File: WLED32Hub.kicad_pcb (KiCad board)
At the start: 2 copper layers, 112.4 x 137.2 mm, 60 parts, among them J1 USB_C_Receptacle_PowerOnly_6P, J10 WAGO, J11 WAGO, J12 WAGO, J13 WAGO, J14 WAGO, J15 WAGO, J16 WAGO, J17 WAGO, J18 WAGO, J19 Conn_01x05, J2 Power WAGO, J3 WAGO, J4 WAGO, J5 WAGO, J6 WAGO, J7 WAGO, J8 WAGO, J9 WAGO, Q1 IRLB8721PBF, Q10 IRLB8721PBF, Q11 IRLB8721PBF, Q12 IRLB8721PBF, Q13 IRLB8721PBF, Q14 IRLB8721PBF, Q15 IRLB8721PBF, Q16 IRLB8721PBF, Q2 IRLB8721PBF, Q3 IRLB8721PBF, Q4 IRLB8721PBF, Q5 IRLB8721PBF, Q6 IRLB8721PBF, Q7 IRLB8721PBF, Q8 IRLB8721PBF, Q9 IRLB8721PBF, U1 ESP32-DevKit-V3.0, U2 Arduino-Pro-Micro

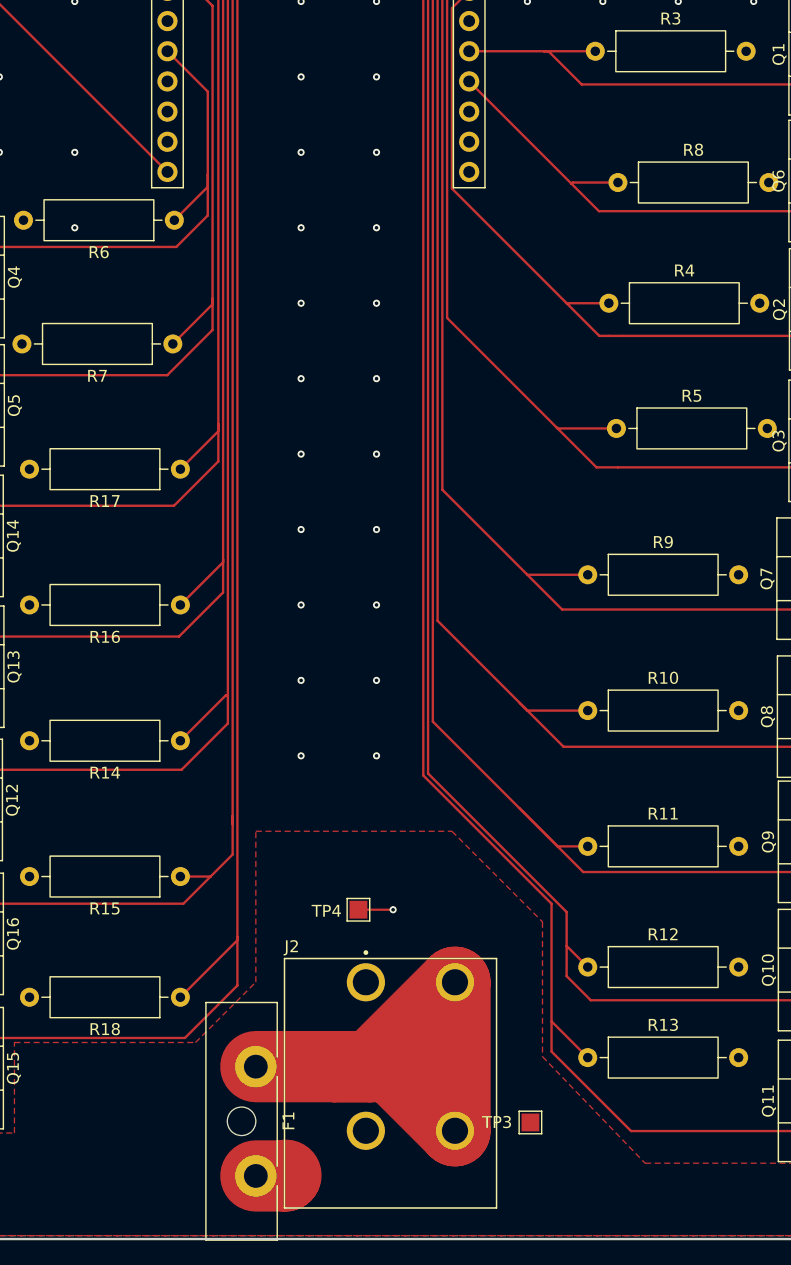
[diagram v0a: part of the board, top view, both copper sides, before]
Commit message: Adding Test Points to LED Switching Signals
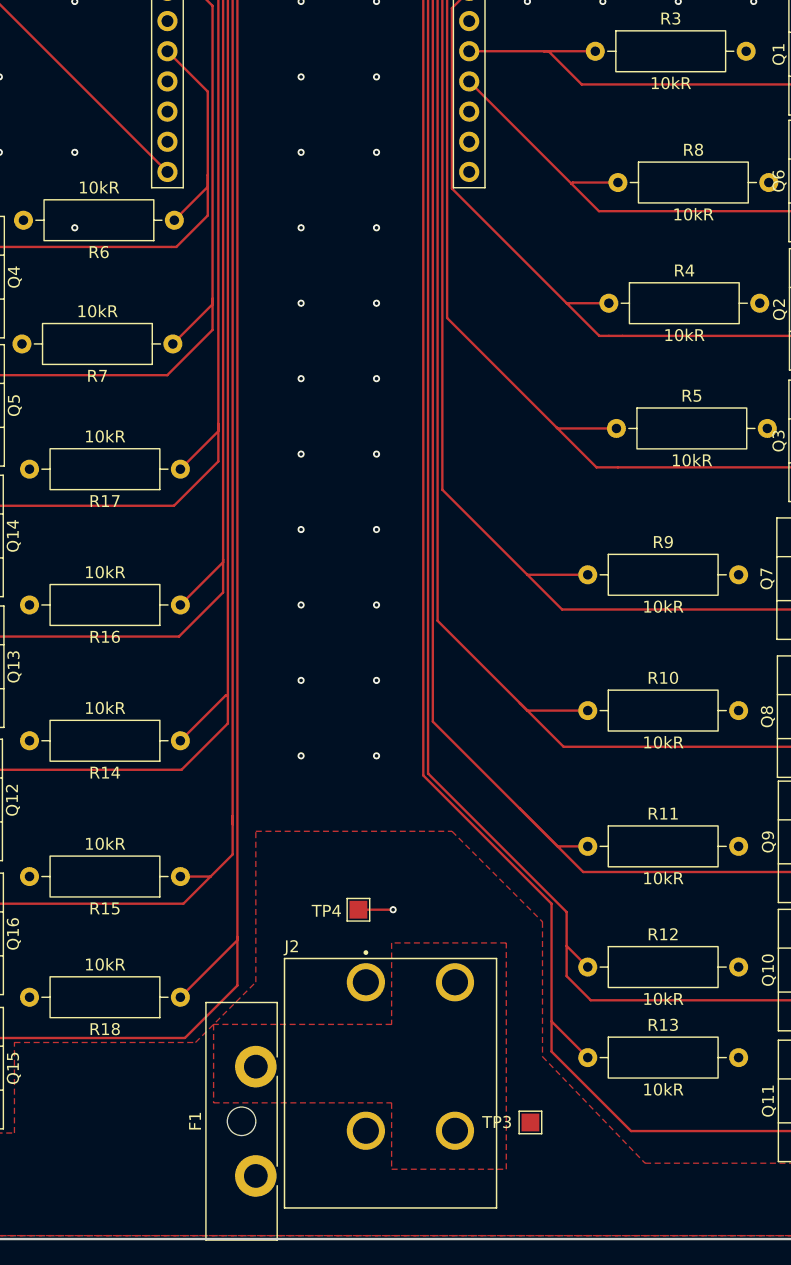
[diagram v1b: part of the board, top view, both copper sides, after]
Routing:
- net Net-(J2-Pin_1): track 44.6 -> 0.00 mm
- net VLED: track 2.56 -> 0.00 mm
- added copper zone on F.Cu, net Net-(J2-Pin_1)
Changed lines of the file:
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@@
 		(property "Value" "10kR"
 			(at 6.35 2.72 0)
-			(layer "F.Fab")
+			(layer "F.SilkS")
 			(effects
 				(font
@@
 		(property "Value" "10kR"
 			(at 6.35 2.72 0)
-			(layer "F.Fab")
+			(layer "F.SilkS")
 			(effects
 				(font
@@
 		(property "Value" "10kR"
 			(at 6.35 2.72 0)
-			(layer "F.Fab")
+			(layer "F.SilkS")
 			(effects
 				(font
@@
 		(property "Value" "10kR"
 			(at 6.35 2.72 0)
-			(layer "F.Fab")
+			(layer "F.SilkS")
 			(effects
 				(font
@@
 		(property "Value" "10kR"
 			(at 6.35 2.72 0)
-			(layer "F.Fab")
+			(layer "F.SilkS")
 			(effects
 				(font
@@
 		(property "Value" "10kR"
 			(at 6.35 2.72 0)
-			(layer "F.Fab")
+			(layer "F.SilkS")
 			(effects
 				(font
@@
 		(tags "Fuseholder ATO Blade littelfuse Pudenz 2 Pin")
 		(property "Reference" "F1"
-			(at 4.57 -2.78 90)
+			(at 4.595 5.08 90)
 			(layer "F.SilkS")
 			(effects
@@
 		(property "Value" "10kR"
 			(at 6.35 2.72 0)
-			(layer "F.Fab")
+			(layer "F.SilkS")
 			(effects
 				(font
@@
 		(property "Value" "10kR"
 			(at 6.35 2.72 0)
-			(layer "F.Fab")
+			(layer "F.SilkS")
 			(effects
 				(font
@@
 		(property "Value" "10kR"
 			(at 6.35 2.72 0)
-			(layer "F.Fab")
+			(layer "F.SilkS")
 			(effects
 				(font
@@
 		(property "Value" "10kR"
 			(at 6.35 2.72 0)
-			(layer "F.Fab")
+			(layer "F.SilkS")
 			(effects
 				(font
@@
 		(property "Value" "10kR"
 			(at 6.35 2.72 0)
-			(layer "F.Fab")
+			(layer "F.SilkS")
 			(effects
 				(font
@@
 		(property "Value" "10kR"
 			(at 6.35 2.72 0)
-			(layer "F.Fab")
+			(layer "F.SilkS")
 			(effects
 				(font
@@
 		(property "Value" "10kR"
 			(at 6.35 2.72 0)
-			(layer "F.Fab")
+			(layer "F.SilkS")
 			(effects
 				(font
@@
 		(property "Value" "10kR"
 			(at 6.35 2.72 0)
-			(layer "F.Fab")
+			(layer "F.SilkS")
 			(effects
 				(font
@@
 		(property "Value" "10kR"
 			(at 6.35 2.72 0)
-			(layer "F.Fab")
+			(layer "F.SilkS")
 			(effects
 				(font
@@
 		(property "Value" "10kR"
 			(at 6.35 2.72 0)
-			(layer "F.Fab")
+			(layer "F.SilkS")
 			(effects
 				(font
@@
 	)
 	(segment
-		(start 129.54 168.712)
-		(end 132.024 168.712)
-		(width 6)
-		(layer "F.Cu")
-		(net 5)
-	)
-	(segment
-		(start 132.024 168.712)
-		(end 132.08 168.656)
-		(width 6)
-		(layer "F.Cu")
-		(net 5)
-	)
-	(segment
 		(start 177.673 74.295)
 		(end 184.333 74.295)
@@
 		(net 73)
 	)
-	(segment
-		(start 129.54 159.512)
-		(end 136.144 159.512)
-		(width 6)
-		(layer "F.Cu")
-		(net 75)
-	)
-	(segment
-		(start 136.144 159.512)
-		(end 140.906 159.512)
-		(width 6)
-		(layer "F.Cu")
-		(net 75)
-	)
-	(segment
-		(start 146.304 152.41)
-		(end 139.202 159.512)
-		(width 6)
-		(layer "F.Cu")
-		(net 75)
-	)
-	(segment
-		(start 146.304 164.91)
-		(end 146.304 152.41)
-		(width 6)
-		(layer "F.Cu")
-		(net 75)
-	)
-	(segment
-		(start 140.906 159.512)
-		(end 146.304 164.91)
-		(width 6)
-		(layer "F.Cu")
-		(net 75)
-	)
-	(segment
-		(start 139.202 159.512)
-		(end 136.144 159.512)
-		(width 6)
-		(layer "F.Cu")
-		(net 75)
-	)
 	(zone
 		(net 5)
@@
 		(fill yes
 			(thermal_gap 0.5)
-			(thermal_bridge_width 0.5)
+			(thermal_bridge_width 1)
 		)
 		(polygon
@@
 			)
 		)
+	)
+	(zone
+		(net 75)
+		(net_name "Net-(J2-Pin_1)")
+		(layer "F.Cu")
+		(hatch edge 0.5)
+		(priority 6)
+		(connect_pads
+			(clearance 0.5)
+		)
+		(min_thickness 0.25)
+		(filled_areas_thickness no)
+		(fill yes
+			(thermal_gap 0.5)
+			(thermal_bridge_width 1)
+			(island_removal_mode 1)
+			(island_area_min 10)
+		)
+		(polygon
+			(pts
+				(xy 125.984 155.956) (xy 125.984 162.56) (xy 140.97 162.56) (xy 140.97 168.148) (xy 150.622 168.148)
+				(xy 150.622 149.098) (xy 140.97 149.098) (xy 140.97 155.956)
+			)
+		)

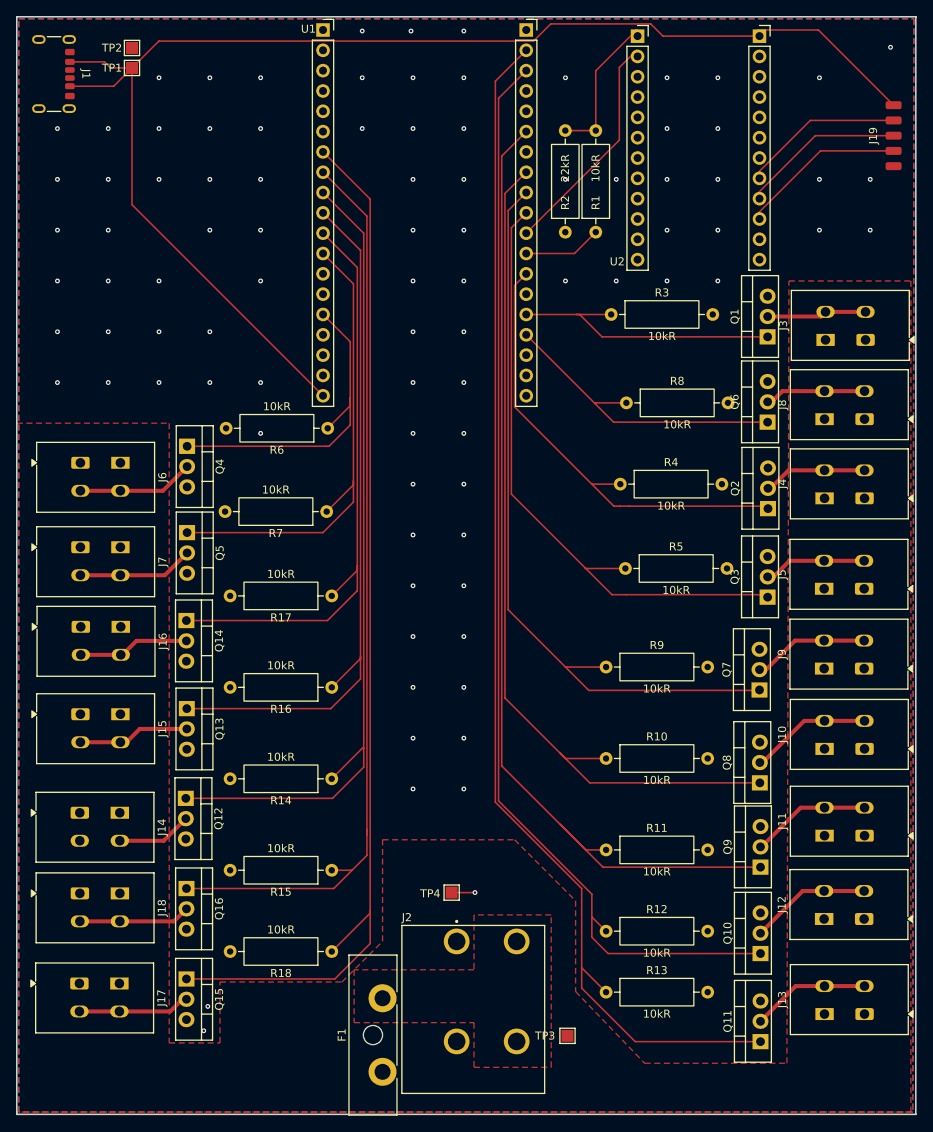
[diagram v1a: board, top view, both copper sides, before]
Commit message: Silkscreen Markers + Test Point Connections
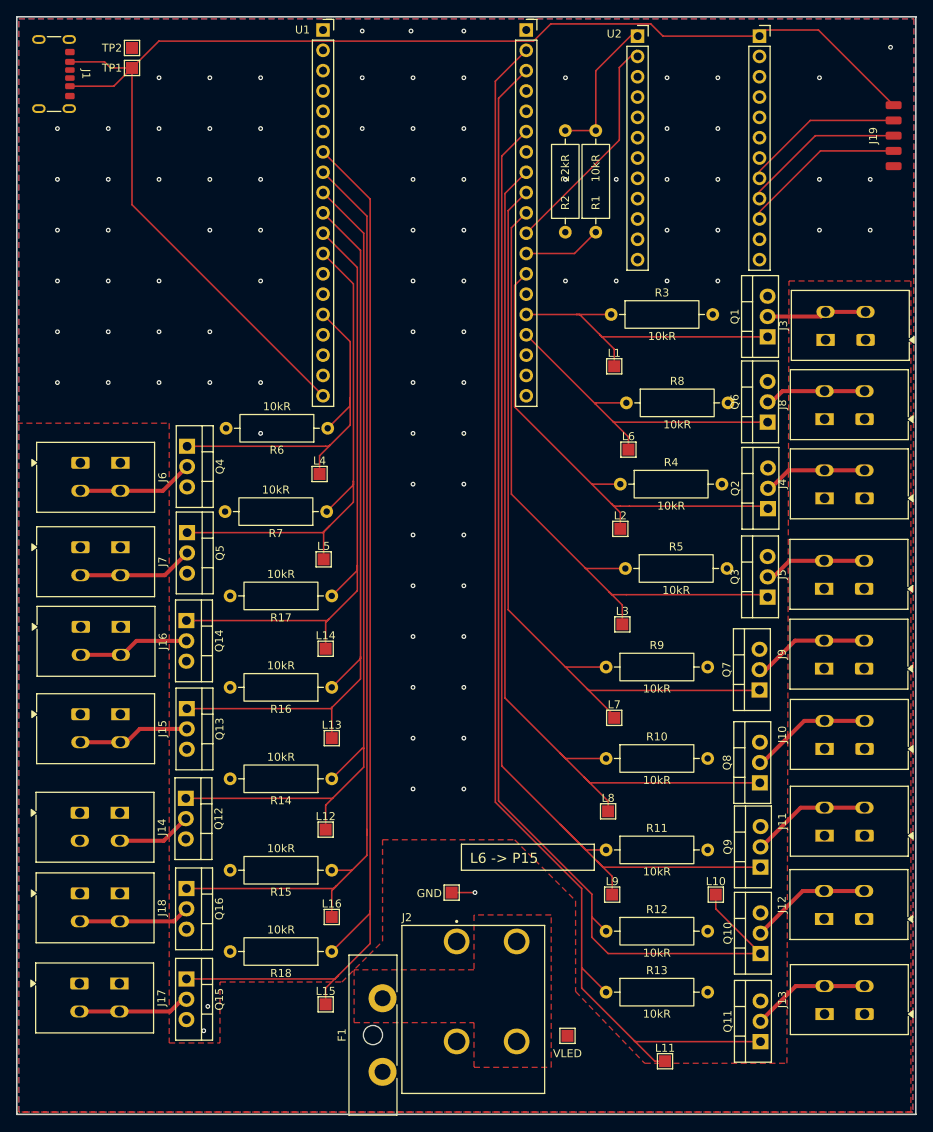
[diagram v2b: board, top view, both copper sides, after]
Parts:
- added L1: TestPoint, TestPoint:TestPoint_Pad_1.5x1.5mm, F.Cu at (158.5, 80.5)
- added L10: TestPoint, TestPoint:TestPoint_Pad_1.5x1.5mm, F.Cu at (171.2, 146.6)
- added L11: TestPoint, TestPoint:TestPoint_Pad_1.5x1.5mm, F.Cu at (164.8, 167.4)
- added L12: TestPoint, TestPoint:TestPoint_Pad_1.5x1.5mm, F.Cu at (122.4, 138.4)
- added L13: TestPoint, TestPoint:TestPoint_Pad_1.5x1.5mm, F.Cu at (123.2, 127.0)
- added L14: TestPoint, TestPoint:TestPoint_Pad_1.5x1.5mm, F.Cu at (122.4, 115.8)
- added L15: TestPoint, TestPoint:TestPoint_Pad_1.5x1.5mm, F.Cu at (122.4, 160.3)
- added L16: TestPoint, TestPoint:TestPoint_Pad_1.5x1.5mm, F.Cu at (123.2, 149.4)
- added L2: TestPoint, TestPoint:TestPoint_Pad_1.5x1.5mm, F.Cu at (159.3, 100.8)
- added L3: TestPoint, TestPoint:TestPoint_Pad_1.5x1.5mm, F.Cu at (159.5, 112.8)
- added L4: TestPoint, TestPoint:TestPoint_Pad_1.5x1.5mm, F.Cu at (121.7, 94.0)
- added L5: TestPoint, TestPoint:TestPoint_Pad_1.5x1.5mm, F.Cu at (122.2, 104.6)
- added L6: TestPoint, TestPoint:TestPoint_Pad_1.5x1.5mm, F.Cu at (160.3, 90.9)
- added L7: TestPoint, TestPoint:TestPoint_Pad_1.5x1.5mm, F.Cu at (158.5, 124.5)
- added L8: TestPoint, TestPoint:TestPoint_Pad_1.5x1.5mm, F.Cu at (157.7, 136.1)
- added L9: TestPoint, TestPoint:TestPoint_Pad_1.5x1.5mm, F.Cu at (158.2, 146.6)
- renumbered TP4 to GND, TP3 to VLED
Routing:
- net LED10: track 139.0 -> 148.7 mm
- net LED8: track 109.1 -> 114.6 mm
- net LED7: track 93.8 -> 98.8 mm
- net LED9: track 125.2 -> 130.1 mm
- net LED11: track 152.7 -> 157.6 mm
- net LED3: track 77.2 -> 82.0 mm
- net LED1: track 36.1 -> 40.8 mm
- net LED5: track 60.2 -> 64.7 mm
- net LED6: track 38.6 -> 43.0 mm
- net LED12: track 103.4 -> 107.6 mm
- net LED15: track 133.3 -> 137.5 mm
- net LED4: track 41.7 -> 45.8 mm
- net LED16: track 115.2 -> 119.3 mm
- net LED13: track 88.7 -> 92.6 mm
- net LED14: track 74.5 -> 78.3 mm
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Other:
- board text added: "L6 -> P15"

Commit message: Fix DRC and Connection Errors
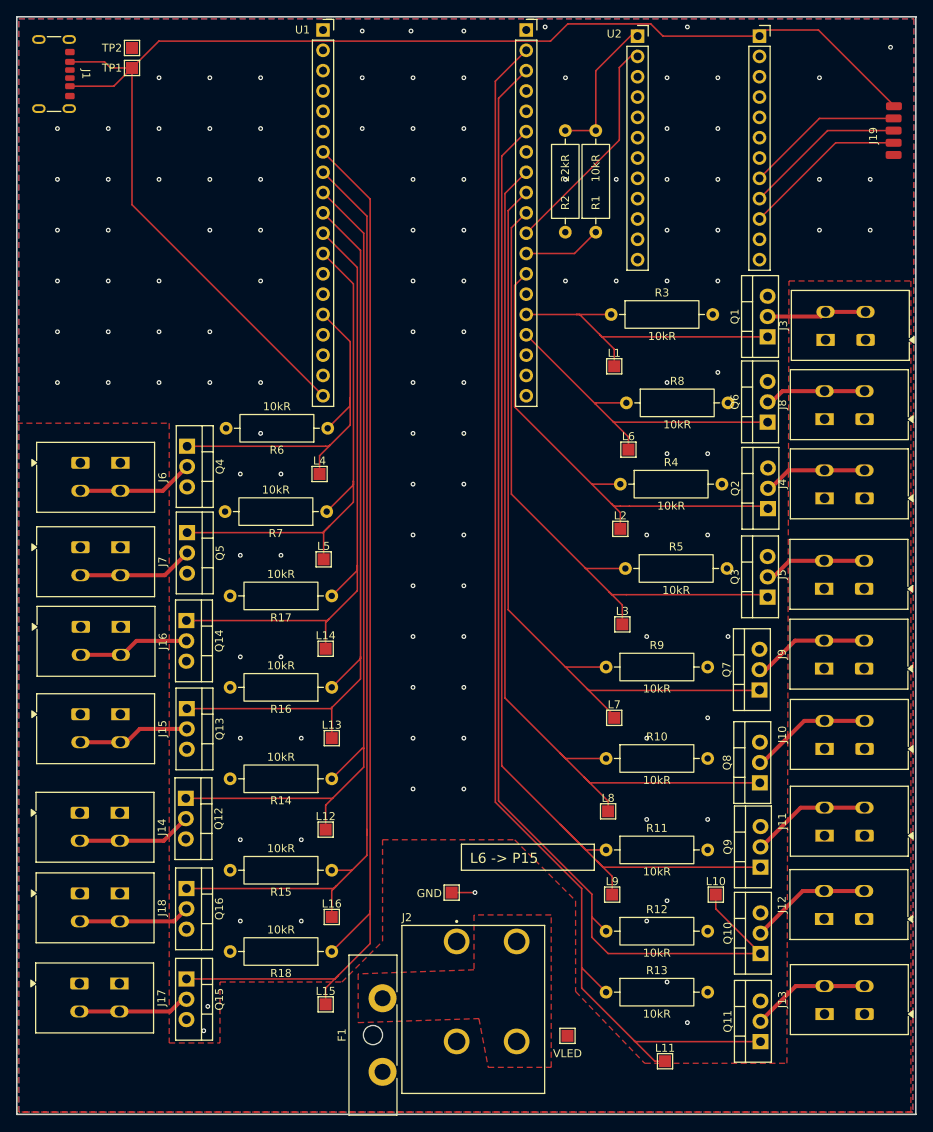
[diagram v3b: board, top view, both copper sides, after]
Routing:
- net GLED12: track 9.40 -> 14.4 mm
- net Net-(J19-Pin_4): track 20.1 -> 20.7 mm
- net GND: track 3.82 -> 3.64 mm, vias 90 -> 120
